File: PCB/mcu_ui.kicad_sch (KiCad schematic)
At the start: 33 parts, among them J5 UPDI, SW1 EC11E18244A5, SW2 BAND, SW3 STEP, SW4 MENU, U4 ATtiny3226-SU

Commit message: DS1 OLED: DNP user-fitted (partial kit), no LCSC, off BOM/pos; keep 3.3V LP2985 rail; silkscreen pin-name note; VERIFY DS1 supply resolved; regen docs
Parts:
- DS1: LCSC C5139764 -> (none); now not fitted; now left out of the parts list
- R20: now not fitted; now left out of the parts list
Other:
- note added: "DS1 DNP: user buys and solders the OLED module (partial kit). Fed 3.3 V from LP2985 OLED rail. PCB: print pin names on silkscreen at DS1 header (GND,VCC,... per final pinout)."
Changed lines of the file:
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@@
 	(text "OLED: SPI only (PA1 MOSI, PA3 SCK, PA4 CS1, PA5 DC). Never shares the Si5351 I2C bus.\nCS2 (font chip) held high by R26."
 		(exclude_from_sim no)
-		(at 255 130 0)
+		(at 255 125.5 0)
+		(effects
+			(font
+				(size 1.27 1.27)
+			)
+			(justify left top)
+		)
+	)
+	(text "DS1 DNP: user buys and solders the OLED module (partial kit). Fed 3.3 V from LP2985 OLED rail.\nPCB: print pin names on silkscreen at DS1 header (GND,VCC,... per final pinout)."
+		(exclude_from_sim no)
+		(at 255 131.5 0)
 		(effects
 			(font
@@
 		(body_style 1)
 		(exclude_from_sim no)
-		(in_bom yes)
+		(in_bom no)
 		(on_board yes)
-		(in_pos_files yes)
-		(dnp no)
+		(in_pos_files no)
+		(dnp yes)
 		(property "Reference" "DS1"
 			(at 299.72 90.17 0)
@@
 			)
 		)
-		(property "Description" "Generic connector, single row, 01x08, script generated (kicad-library-utils/schlib/autogen/connector/)"
+		(property "Description" "1.3in SH1106 SPI OLED module, user-fitted (DNP, partial kit). Footprint/pinout currently HS13L01W4S01 8-pin: GND,VCC,SCL,SDA,DC,CS1,FS0,CS2"
 			(at 299.72 100.33 0)
 			(hide yes)
@@
 			)
 		)
-		(property "LCSC" "C5139764"
+		(property "LCSC" ""
 			(at 299.72 100.33 0)
 			(hide yes)
@@
 		(body_style 1)
 		(exclude_from_sim no)
-		(in_bom yes)
+		(in_bom no)
 		(on_board yes)
-		(in_pos_files yes)
-		(dnp no)
+		(in_pos_files no)
+		(dnp yes)
 		(property "Reference" "R20"
 			(at 236.75 201.33 0)

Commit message: DS1: generic 1.3in SH1106 SPI 7-pin (GND,VCC,CLK,MOSI,RES,DC,CS); OLED_RES on PA6, PA2 freed; remove R26/FS0/CS2; DNP supplied in kit; VERIFY + regen docs
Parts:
- removed R26: 10k, Resistor_SMD:R_0805_2012Metric, symbol Device:R_Small_US
- DS1: value HS13L01W4S01 -> OLED_1.3in_SH1106_SPI_7pin; footprint Connector_PinHeader_2.54mm:PinHeader_1x08_P2.54mm_Vertical -> Connector_PinHeader_2.54mm:PinHeader_1x07_P2.54mm_Vertical; symbol Connector_Generic:Conn_01x08 -> Connector_Generic:Conn_01x07; MPN HS13L01W4S01 -> generic 1.3in SH1106 SPI 7-pin; Manufacturer HS -> generic
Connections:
- net OLED_DC: now also DS1.6 (Pin_6); no longer DS1.5 (Pin_5)
- net OLED_CS1 renamed OLED_CS
- net OLED_CS: now also DS1.7 (Pin_7); no longer DS1.6 (Pin_6)
- net OLED_CS2 renamed OLED_RES
- net OLED_RES: now also DS1.5 (Pin_5); no longer DS1.8 (Pin_8)
- net OLED_FS0: no longer names the net of U4.18 (PA2)
- net OLED_FS0: no longer DS1.7 (Pin_7)
- no-connect marks 0 -> 1
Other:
- note added: "DS1 DNP: OLED module supplied in kit, user-soldered. Fed 3.3 V from LP2985 OLED rail. PCB: print pin names on silkscreen at DS1 header (GND,VCC,CLK,MOSI,RES,DC,CS); suppliers vary."
- note added: "OLED: SPI only (PA1 MOSI, PA3 SCK, PA4 CS, PA5 DC, PA6 RES). Never shares the Si5351 I2C bus. PA2 spare (no-connect)."
- note removed: "DS1 DNP: user buys and solders the OLED module (partial kit). Fed 3.3 V from LP2985 OLED rail. PCB: print pin names on silkscreen at DS1 header (GND,VCC,... per final pinout)."
- note removed: "OLED: SPI only (PA1 MOSI, PA3 SCK, PA4 CS1, PA5 DC). Never shares the Si5351 I2C bus. CS2 (font chip) held high by R26."
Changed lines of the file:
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@@
 		)
 	)
-	(text "OLED: SPI only (PA1 MOSI, PA3 SCK, PA4 CS1, PA5 DC). Never shares the Si5351 I2C bus.\nCS2 (font chip) held high by R26."
+	(text "OLED: SPI only (PA1 MOSI, PA3 SCK, PA4 CS, PA5 DC, PA6 RES). Never shares the Si5351 I2C bus.\nPA2 spare (no-connect)."
 		(exclude_from_sim no)
 		(at 255 125.5 0)
@@
 		)
 	)
-	(text "DS1 DNP: user buys and solders the OLED module (partial kit). Fed 3.3 V from LP2985 OLED rail.\nPCB: print pin names on silkscreen at DS1 header (GND,VCC,... per final pinout)."
+	(text "DS1 DNP: OLED module supplied in kit, user-soldered. Fed 3.3 V from LP2985 OLED rail.\nPCB: print pin names on silkscreen at DS1 header (GND,VCC,CLK,MOSI,RES,DC,CS); suppliers vary."
 		(exclude_from_sim no)
 		(at 255 131.5 0)
@@
 		)
 	)
+	(no_connect
+		(at 165.1 97.79)
+	)
 	(label "ENC_SW_SW"
 		(at 57.15 257.81 0)
@@
 		)
 	)
-	(label "OLED_FS0"
+	(label "OLED_CS"
 		(at 294.64 107.95 180)
 		(effects
@@
 		)
 	)
-	(label "OLED_CS1"
+	(label "OLED_DC"
 		(at 294.64 105.41 180)
 		(effects
@@
 		)
 	)
-	(label "OLED_DC"
+	(label "OLED_RES"
 		(at 294.64 102.87 180)
 		(effects
@@
 		)
 	)
-	(label "OLED_FS0"
-		(at 165.1 97.79 0)
-		(effects
-			(font
-				(size 1.27 1.27)
-			)
-			(justify left bottom)
-		)
-	)
 	(label "ENC_B"
 		(at 134.62 118.11 180)
@@
 		)
 	)
-	(label "OLED_CS2"
-		(at 270.51 72.39 270)
-		(effects
-			(font
-				(size 1.27 1.27)
-			)
-			(justify right bottom)
-		)
-	)
 	(label "ENC_B_SW"
 		(at 41.91 262.89 180)
@@
 		)
 	)
-	(label "OLED_CS2"
+	(label "OLED_RES"
 		(at 165.1 107.95 0)
 		(effects
@@
 		)
 	)
-	(label "OLED_CS2"
-		(at 294.64 110.49 180)
-		(effects
-			(font
-				(size 1.27 1.27)
-			)
-			(justify right bottom)
-		)
-	)
 	(label "BTN_STEP_SW"
 		(at 134.62 260.35 180)
@@
 		)
 	)
-	(label "OLED_CS1"
+	(label "OLED_CS"
 		(at 165.1 102.87 0)
 		(effects
@@
 	)
 	(symbol
-		(lib_id "Connector_Generic:Conn_01x08")
+		(lib_id "Connector_Generic:Conn_01x07")
 		(at 299.72 100.33 0)
 		(unit 1)
@@
 			)
 		)
-		(property "Value" "HS13L01W4S01"
+		(property "Value" "OLED_1.3in_SH1106_SPI_7pin"
 			(at 299.72 113.03 0)
 			(show_name no)
@@
 			)
 		)
-		(property "Footprint" "Connector_PinHeader_2.54mm:PinHeader_1x08_P2.54mm_Vertical"
+		(property "Footprint" "Connector_PinHeader_2.54mm:PinHeader_1x07_P2.54mm_Vertical"
 			(at 299.72 100.33 0)
 			(hide yes)
@@
 			)
 		)
-		(property "Description" "1.3in SH1106 SPI OLED module, user-fitted (DNP, partial kit). Footprint/pinout currently HS13L01W4S01 8-pin: GND,VCC,SCL,SDA,DC,CS1,FS0,CS2"
+		(property "Description" "Generic 1.3in 128x64 SH1106 4-wire SPI OLED module, 7-pin 2.54 mm: GND,VCC,CLK(D0),MOSI(D1),RES,DC,CS. DNP, supplied in kit, user-soldered."
 			(at 299.72 100.33 0)
 			(hide yes)
@@
 			)
 		)
-		(property "MPN" "HS13L01W4S01"
+		(property "MPN" "generic 1.3in SH1106 SPI 7-pin"
 			(at 299.72 100.33 0)
 			(hide yes)
@@
 			)
 		)
-		(property "Manufacturer" "HS"
+		(property "Manufacturer" "generic"
 			(at 299.72 100.33 0)
 			(hide yes)
@@
 		(pin "7"
 		)
-		(pin "8"
-		)
 		(instances
 			(project "Si5351AVFO"
@@
 	)
 	(symbol
-		(lib_id "power:+3V3")
-		(at 270.51 67.31 0)
-		(unit 1)
-		(body_style 1)
-		(exclude_from_sim no)
-		(in_bom no)
-		(on_board yes)
-		(in_pos_files yes)
-		(dnp no)
-		(property "Reference" "#PWR062"
-			(at 270.51 67.31 0)
-			(hide yes)
-			(show_name no)
-			(do_not_autoplace no)
-			(effects
-				(font
-					(size 1.27 1.27)
-				)
-			)
-		)
-		(property "Value" "+3V3D"
-			(at 270.51 63.5 0)
-			(show_name no)
-			(do_not_autoplace no)
-			(effects
-				(font
-					(size 1.27 1.27)
-				)
-			)
-		)
-		(property "Footprint" ""
-			(at 270.51 67.31 0)
-			(hide yes)
-			(show_name no)
-			(do_not_autoplace no)
-			(effects
-				(font
-					(size 1.27 1.27)
-				)
-			)
-		)
-		(property "Datasheet" ""
-			(at 270.51 67.31 0)
-			(hide yes)
-			(show_name no)
-			(do_not_autoplace no)
-			(effects
-				(font
-					(size 1.27 1.27)
-				)
-			)
-		)
-		(property "Description" ""
-			(at 270.51 67.31 0)
-			(show_name no)
-			(do_not_autoplace no)
-			(effects
-				(font
-					(size 1.27 1.27)
-				)
-			)
-		)
-		(pin "1"
-		)
-		(instances
-			(project "Si5351AVFO"
-				(path "/a0000000-0000-4000-8000-000000000001/b0000000-0000-4000-8000-000000000003"
-					(reference "#PWR062")
-					(unit 1)
-				)
-			)
-		)
-	)
-	(symbol
 		(lib_id "power:GND")
 		(at 124.46 224.79 0)
@@
 					(unit 1)
 				)
-			)
-		)
-	)
-	(symbol
-		(lib_id "Device:R_Small_US")
-		(at 270.51 69.85 0)
-		(unit 1)
-		(body_style 1)
-		(exclude_from_sim no)
-		(in_bom yes)
-		(on_board yes)
-		(in_pos_files yes)
-		(dnp no)
-		(property "Reference" "R26"
-			(at 272.31 69.25 0)
-			(show_name no)
-			(do_not_autoplace no)
-			(effects
-				(font
-					(size 1.27 1.27)
-				)
-				(justify left)
-			)
-		)
-		(property "Value" "10k"
-			(at 272.31 71.45 0)
-			(show_name no)
-			(do_not_autoplace no)
-			(effects
-				(font
-					(size 1.27 1.27)
-				)
-				(justify left)
-			)
-		)
-		(property "Footprint" "Resistor_SMD:R_0805_2012Metric"
-			(at 270.51 69.85 0)
-			(hide yes)
-			(show_name no)
-			(do_not_autoplace no)
-			(effects
-				(font
-					(size 1.27 1.27)
-				)
-			)
-		)
-		(property "Datasheet" ""
-			(at 270.51 69.85 0)
-			(hide yes)
-			(show_name no)
-			(do_not_autoplace no)
-			(effects
-				(font
-					(size 1.27 1.27)
-				)
-			)
-		)
-		(property "Description" "Resistor, small symbol"
-			(at 270.51 69.85 0)
-			(hide yes)
-			(show_name no)
-			(do_not_autoplace no)
-			(effects
-				(font
-					(size 1.27 1.27)
-				)
-			)
-		)
-		(property "LCSC" "C17414"
-			(at 270.51 69.85 0)
-			(hide yes)
-			(show_name no)
-			(do_not_autoplace no)
-			(effects
-				(font
-					(size 1.27 1.27)
-				)
-			)
-		)
-		(property "MPN" "0805W8F1002T5E"
-			(at 270.51 69.85 0)
-			(hide yes)
-			(show_name no)
-			(do_not_autoplace no)
-			(effects
-				(font
-					(size 1.27 1.27)
-				)
-			)
-		)
-		(property "Manufacturer" "UNI-ROYAL"
-			(at 270.51 69.85 0)
-			(hide yes)
-			(show_name no)
-			(do_not_autoplace no)
-			(effects
-				(font
-					(size 1.27 1.27)
-				)
-			)
-		)
-		(pin "1"
-		)
-		(pin "2"
-		)
-		(instances
-			(project "Si5351AVFO"
-				(path "/a0000000-0000-4000-8000-000000000001/b0000000-0000-4000-8000-000000000003"
-					(reference "R26")
-					(unit 1)
-				)

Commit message: SW2-SW4: 6x6 mm 11 mm-tall SMD tact switch KH-6X6X11H-STM (C2837537) for front panel
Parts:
- SW2, SW3, SW4: footprint Button_Switch_SMD:SW_Push_1P1T_XKB_TS-1187A -> EtherkitKicadLibrary:SW_Push_6x6mm_SMD_KH-6X6X11H-STM; LCSC C318884 -> C2837537; MPN TS-1187A-B-A-B -> KH-6X6X11H-STM; Manufacturer XKB -> Kinghelm
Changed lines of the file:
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@@
 			)
 		)
-		(property "Footprint" "Button_Switch_SMD:SW_Push_1P1T_XKB_TS-1187A"
+		(property "Footprint" "EtherkitKicadLibrary:SW_Push_6x6mm_SMD_KH-6X6X11H-STM"
 			(at 110.49 260.35 0)
 			(hide yes)
@@
 			)
 		)
-		(property "Description" "Push button switch, generic, two pins"
+		(property "Description" "Tactile switch 6x6 mm SMD, 11 mm actuator (front-panel height, no cap)"
 			(at 110.49 260.35 0)
 			(hide yes)
@@
 			)
 		)
-		(property "LCSC" "C318884"
+		(property "LCSC" "C2837537"
 			(at 110.49 260.35 0)
 			(hide yes)
@@
 			)
 		)
-		(property "MPN" "TS-1187A-B-A-B"
+		(property "MPN" "KH-6X6X11H-STM"
 			(at 110.49 260.35 0)
 			(hide yes)
@@
 			)
 		)
-		(property "Manufacturer" "XKB"
+		(property "Manufacturer" "Kinghelm"
 			(at 110.49 260.35 0)
 			(hide yes)
@@
 			)
 		)
-		(property "Footprint" "Button_Switch_SMD:SW_Push_1P1T_XKB_TS-1187A"
+		(property "Footprint" "EtherkitKicadLibrary:SW_Push_6x6mm_SMD_KH-6X6X11H-STM"
 			(at 170.18 260.35 0)
 			(hide yes)
@@
 			)
 		)
-		(property "Description" "Push button switch, generic, two pins"
+		(property "Description" "Tactile switch 6x6 mm SMD, 11 mm actuator (front-panel height, no cap)"
 			(at 170.18 260.35 0)
 			(hide yes)
@@
 			)
 		)
-		(property "LCSC" "C318884"
+		(property "LCSC" "C2837537"
 			(at 170.18 260.35 0)
 			(hide yes)
@@
 			)
 		)
-		(property "MPN" "TS-1187A-B-A-B"
+		(property "MPN" "KH-6X6X11H-STM"
 			(at 170.18 260.35 0)
 			(hide yes)
@@
 			)
 		)
-		(property "Manufacturer" "XKB"
+		(property "Manufacturer" "Kinghelm"
 			(at 170.18 260.35 0)
 			(hide yes)
@@
 			)
 		)
-		(property "Footprint" "Button_Switch_SMD:SW_Push_1P1T_XKB_TS-1187A"
+		(property "Footprint" "EtherkitKicadLibrary:SW_Push_6x6mm_SMD_KH-6X6X11H-STM"
 			(at 139.7 260.35 0)
 			(hide yes)
@@
 			)
 		)
-		(property "Description" "Push button switch, generic, two pins"
+		(property "Description" "Tactile switch 6x6 mm SMD, 11 mm actuator (front-panel height, no cap)"
 			(at 139.7 260.35 0)
 			(hide yes)
@@
 			)
 		)
-		(property "LCSC" "C318884"
+		(property "LCSC" "C2837537"
 			(at 139.7 260.35 0)
 			(hide yes)
@@
 			)
 		)
-		(property "MPN" "TS-1187A-B-A-B"
+		(property "MPN" "KH-6X6X11H-STM"
 			(at 139.7 260.35 0)
 			(hide yes)
@@
 			)
 		)
-		(property "Manufacturer" "XKB"
+		(property "Manufacturer" "Kinghelm"
 			(at 139.7 260.35 0)
 			(hide yes)

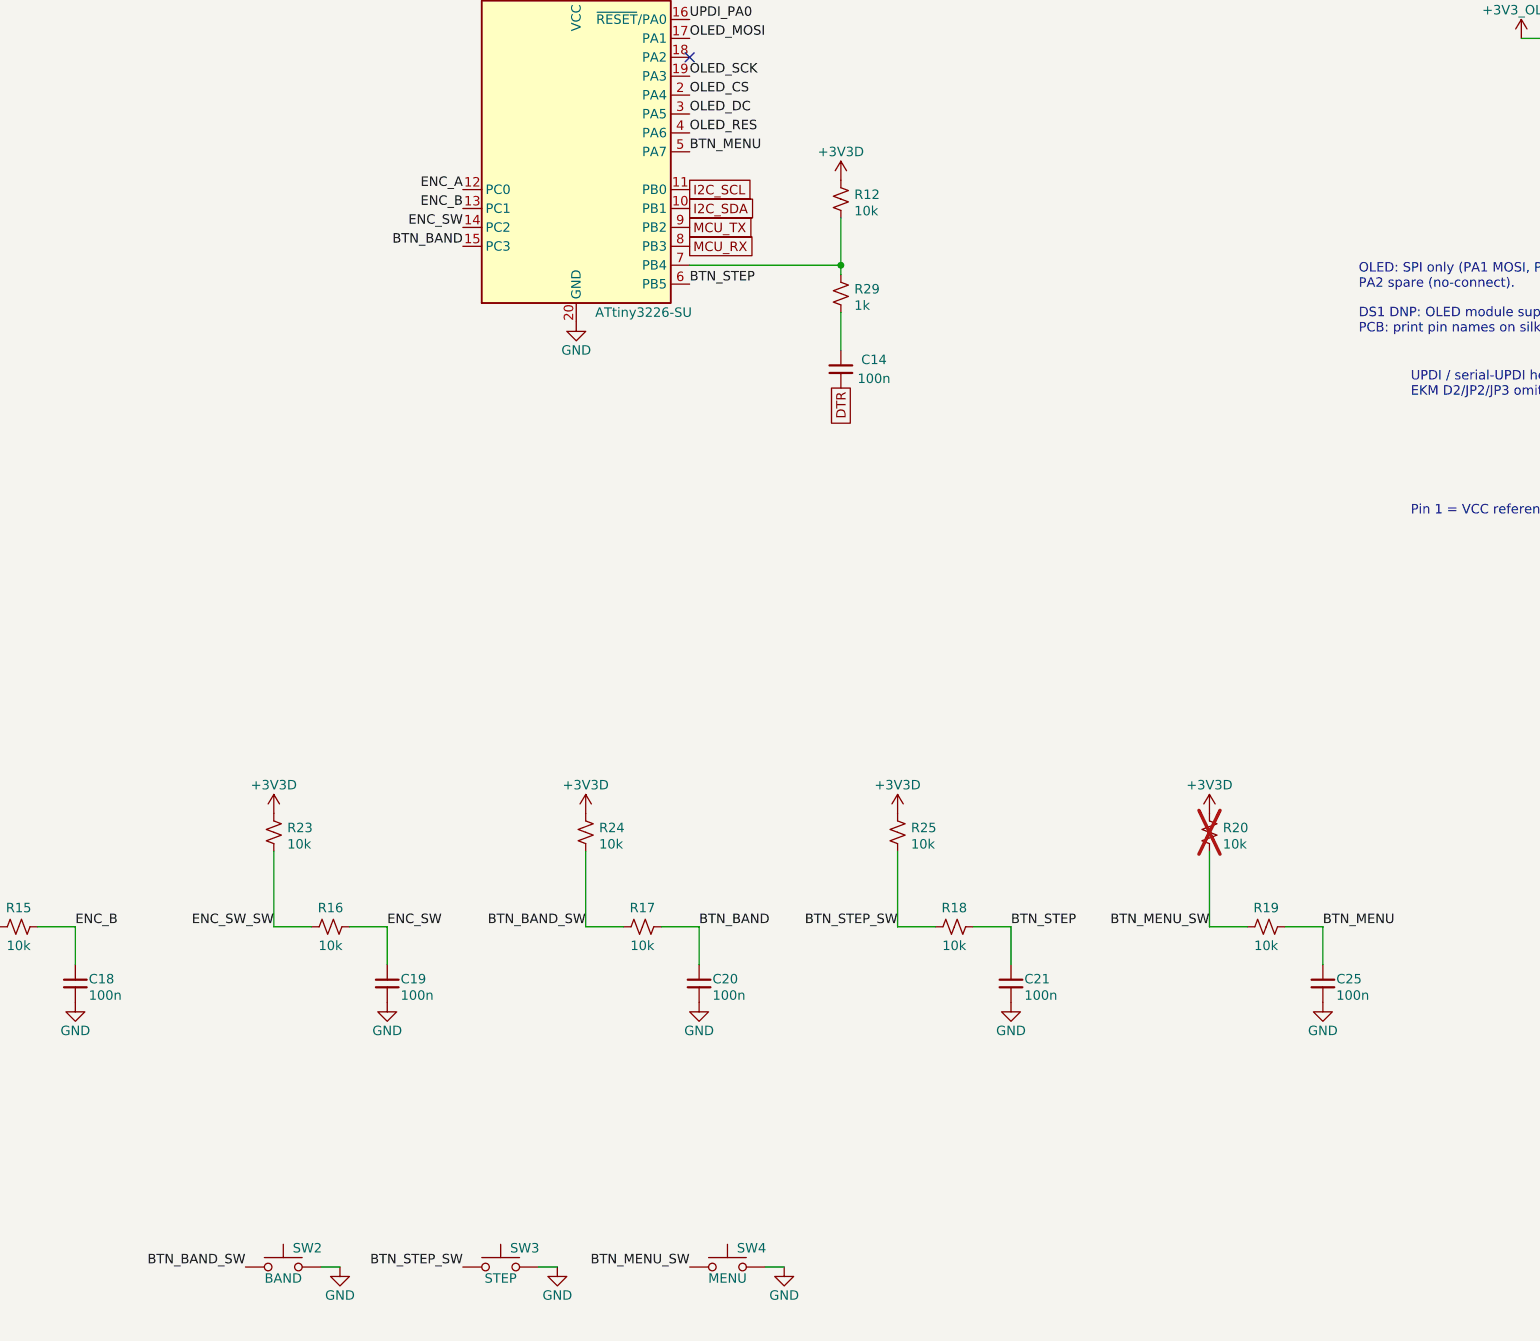
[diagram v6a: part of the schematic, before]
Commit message: Sync schematic from rev-a-schematic (a9b48d3): soft-button nets BTN_S1-S3, SW2-SW4 SOFT1-3; regen docs
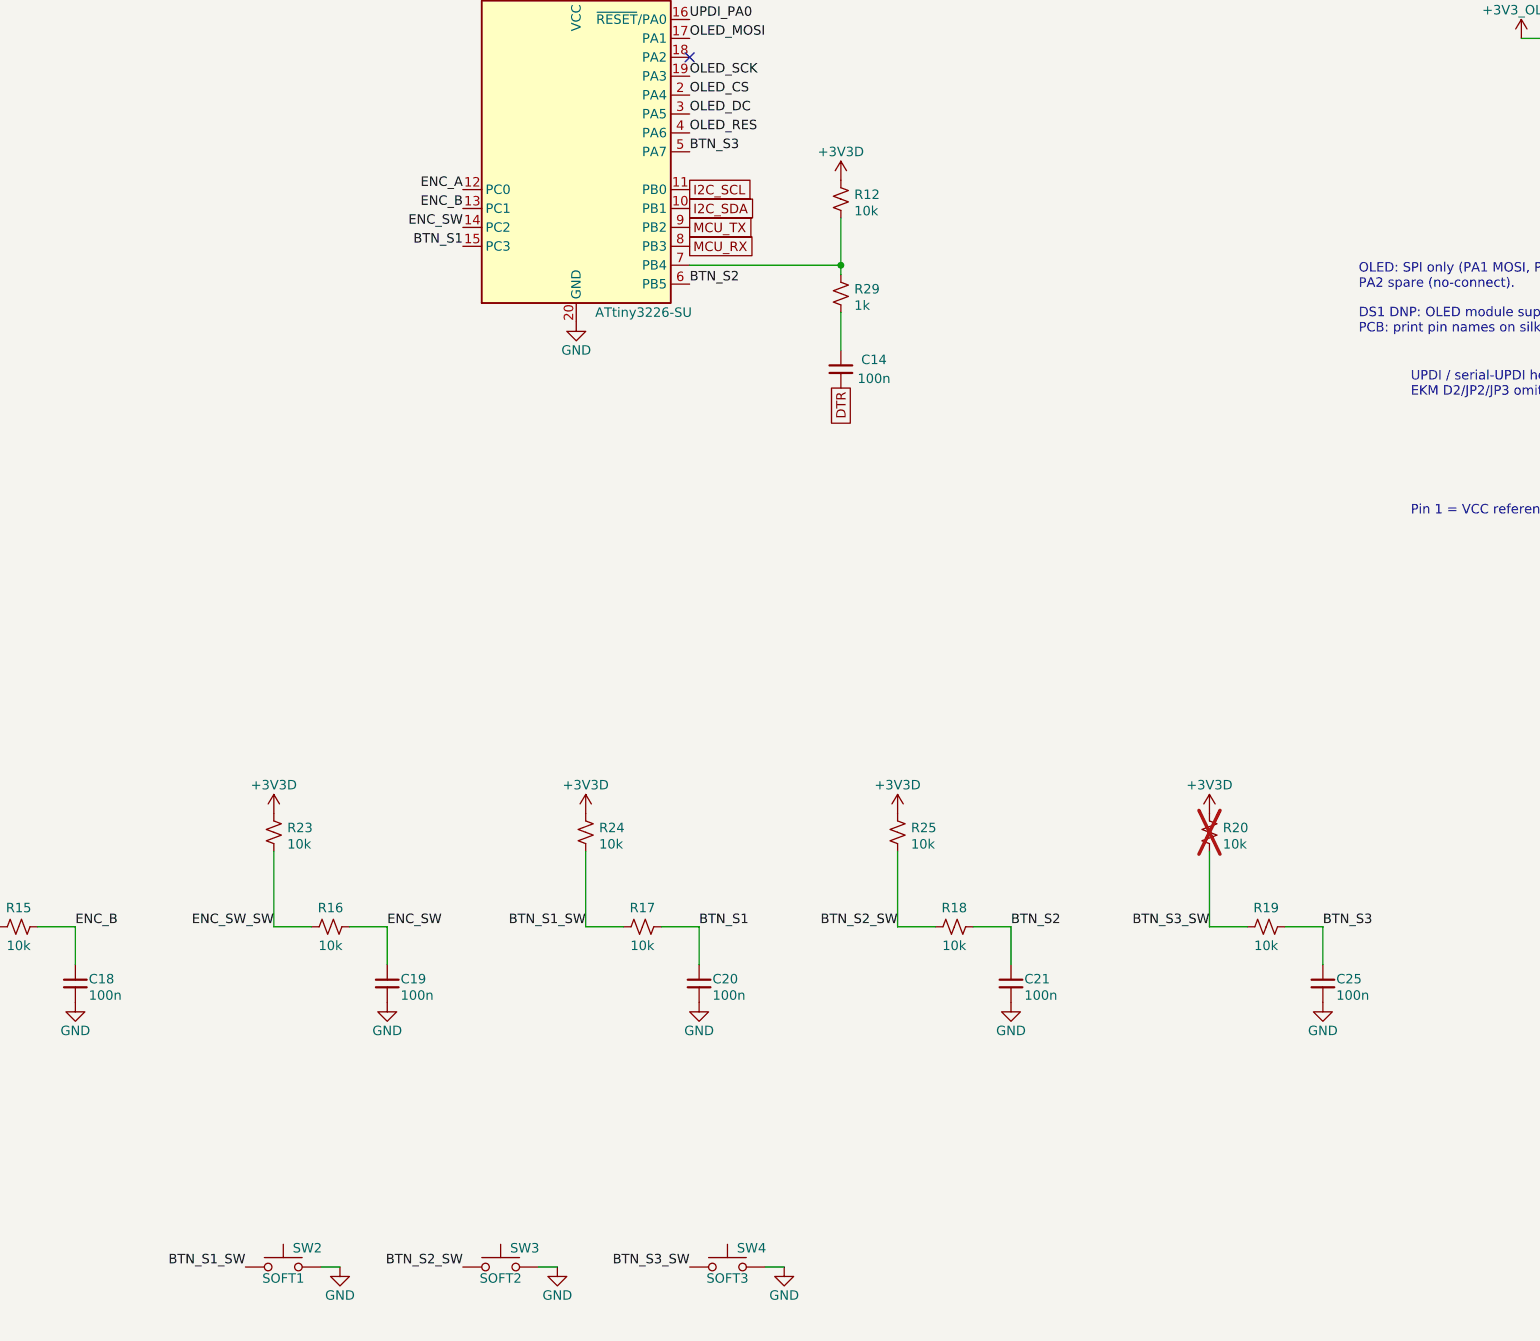
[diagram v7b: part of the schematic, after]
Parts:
- SW2: value BAND -> SOFT1
- SW3: value STEP -> SOFT2
- SW4: value MENU -> SOFT3
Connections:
- net BTN_BAND renamed BTN_S1
- net BTN_BAND_SW renamed BTN_S1_SW
- net BTN_MENU renamed BTN_S3
- net BTN_MENU_SW renamed BTN_S3_SW
- net BTN_STEP renamed BTN_S2
- net BTN_STEP_SW renamed BTN_S2_SW
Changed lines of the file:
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@@
 		)
 	)
-	(label "BTN_MENU"
+	(label "BTN_S3"
 		(at 165.1 110.49 0)
 		(effects
@@
 		)
 	)
-	(label "BTN_BAND"
+	(label "BTN_S1"
 		(at 166.37 214.63 0)
 		(effects
@@
 		)
 	)
-	(label "BTN_BAND"
+	(label "BTN_S1"
 		(at 134.62 123.19 180)
 		(effects
@@
 		)
 	)
-	(label "BTN_MENU_SW"
+	(label "BTN_S3_SW"
 		(at 165.1 260.35 180)
 		(effects
@@
 		)
 	)
-	(label "BTN_BAND_SW"
+	(label "BTN_S1_SW"
 		(at 151.13 214.63 180)
 		(effects
@@
 		)
 	)
-	(label "BTN_STEP_SW"
+	(label "BTN_S2_SW"
 		(at 193.04 214.63 180)
 		(effects
@@
 		)
 	)
-	(label "BTN_STEP"
+	(label "BTN_S2"
 		(at 165.1 128.27 0)
 		(effects
@@
 		)
 	)
-	(label "BTN_BAND_SW"
+	(label "BTN_S1_SW"
 		(at 105.41 260.35 180)
 		(effects
@@
 		)
 	)
-	(label "BTN_MENU_SW"
+	(label "BTN_S3_SW"
 		(at 234.95 214.63 180)
 		(effects
@@
 		)
 	)
-	(label "BTN_STEP_SW"
+	(label "BTN_S2_SW"
 		(at 134.62 260.35 180)
 		(effects
@@
 		)
 	)
-	(label "BTN_MENU"
+	(label "BTN_S3"
 		(at 250.19 214.63 0)
 		(effects
@@
 		)
 	)
-	(label "BTN_STEP"
+	(label "BTN_S2"
 		(at 208.28 214.63 0)
 		(effects
@@
 			)
 		)
-		(property "Value" "BAND"
+		(property "Value" "SOFT1"
 			(at 110.49 261.874 0)
 			(show_name no)
@@
 			)
 		)
-		(property "Value" "MENU"
+		(property "Value" "SOFT3"
 			(at 170.18 261.874 0)
 			(show_name no)
@@
 			)
 		)
-		(property "Value" "STEP"
+		(property "Value" "SOFT2"
 			(at 139.7 261.874 0)
 			(show_name no)
